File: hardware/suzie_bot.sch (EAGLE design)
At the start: 39 parts, among them IC1 LT1529CT33, IC2 L9637D, IC3 IC_TXB0108-TSSOP-20, U1 ATMEGA1284P-AU, Y1 14.7456, Y2 6.0, Y3 16.0

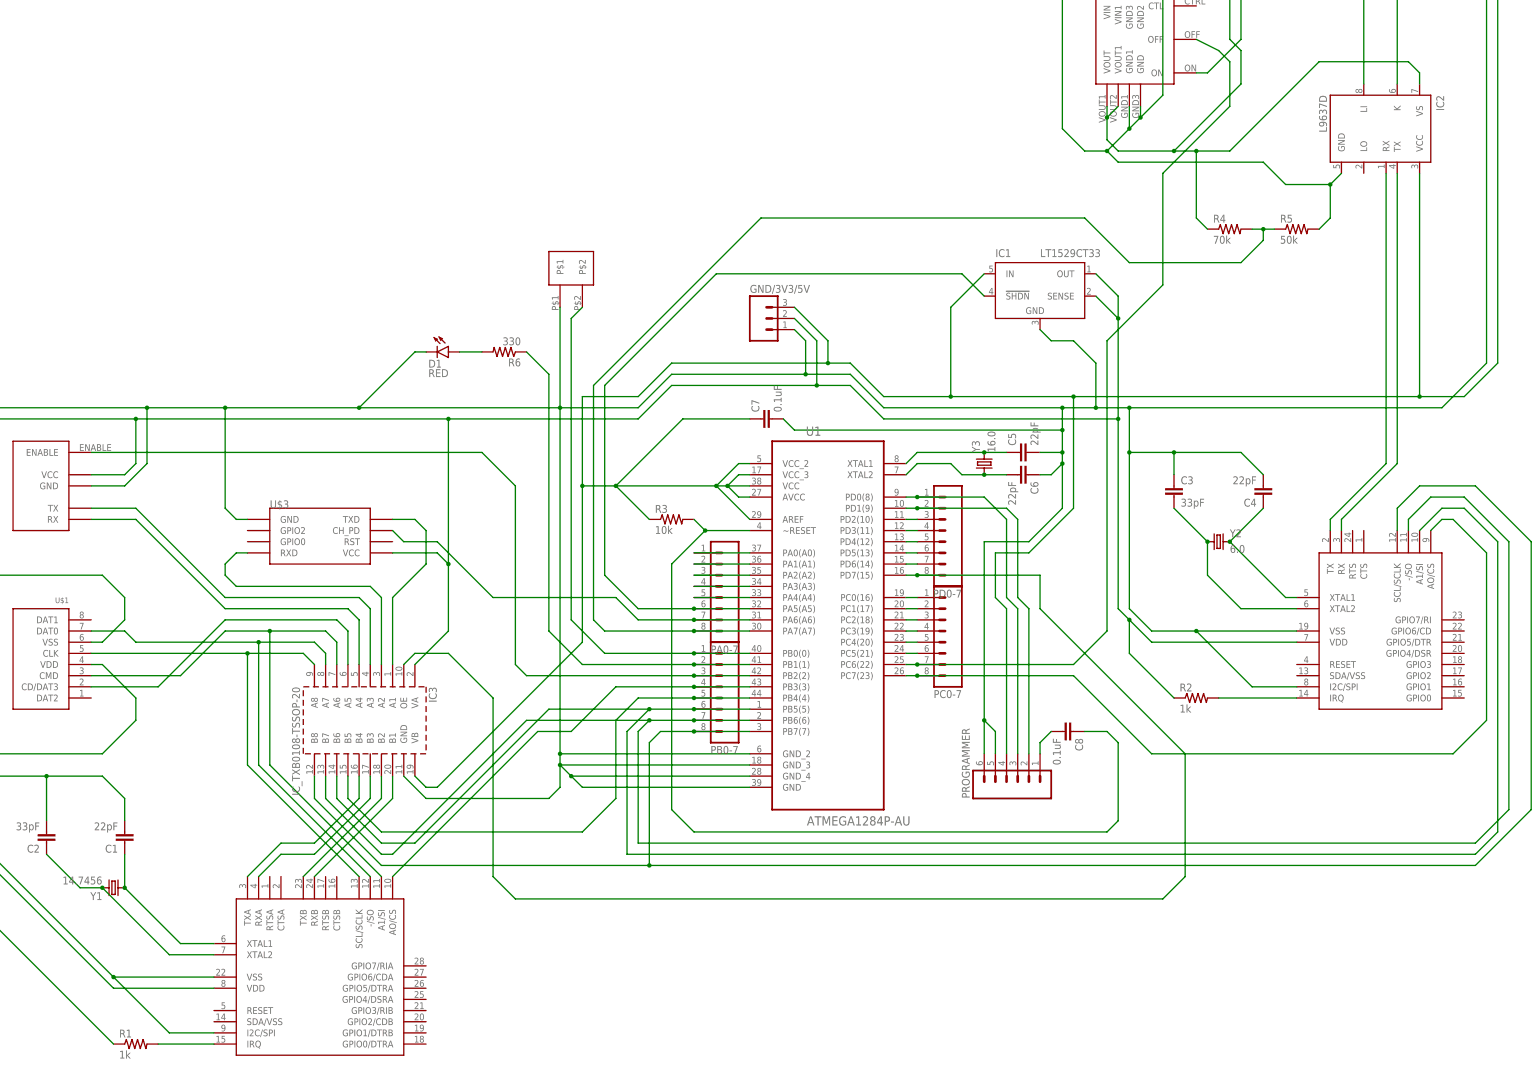
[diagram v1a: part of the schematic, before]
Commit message: Updating to v1.3 boardfile (what was once an atmega328p is now an atmega1284p)
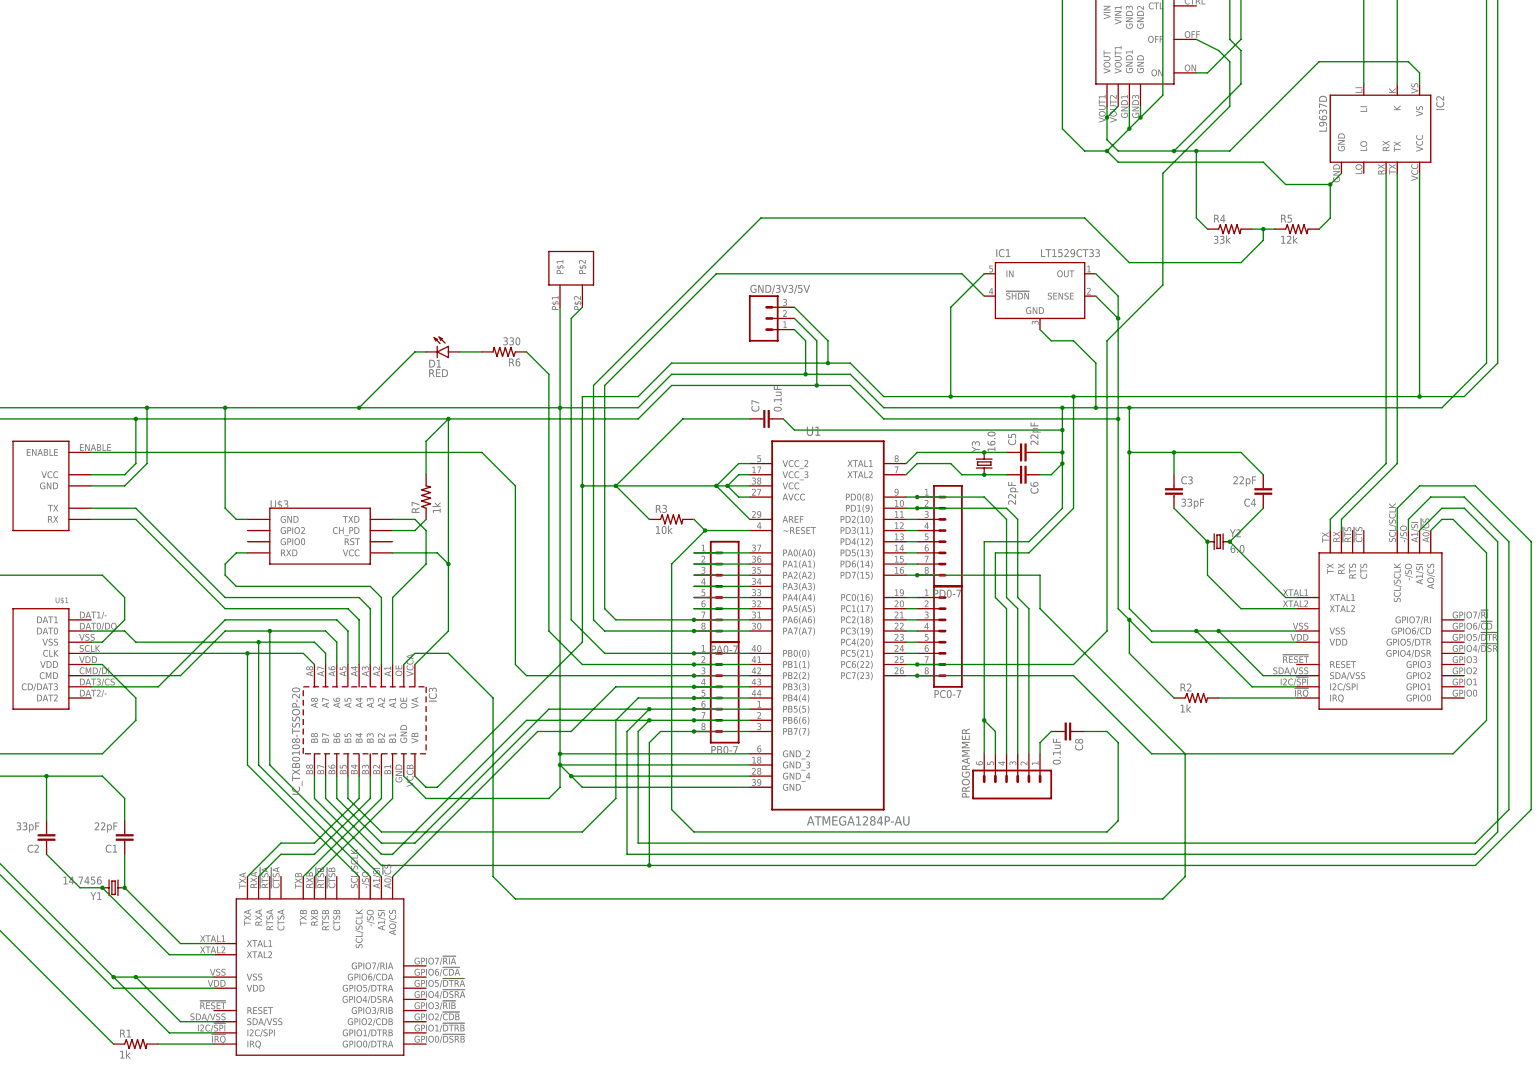
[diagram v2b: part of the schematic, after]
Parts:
- added R7: 1k, SparkFun-Passives:RESISTOR0805-RES
- R4: value 70k -> 33k
- R5: value 50k -> 12k
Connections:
- removed net PA5: IC1.!SHDN, PA0-7.6, U1.PA5(A5)
- new net N$28: PA0-7.6, U1.PA5(A5)
- new net N$4: R7.1, U$3.CH_PD
- net 3V3: now also R7.2
- net GND: now also U$2.SDA/VSS, U$7.SDA/VSS
- net PA6: now also IC1.!SHDN; no longer U$3.CH_PD
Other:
- moved on the sheet: IC2, U$1
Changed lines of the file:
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@@
 <part name="C8" library="SparkFun-Passives" deviceset="CAP" device="0805" value="0.1uF"/>
 <part name="IC3" library="dp_devices.v6" deviceset="IC_TXB0108" device="-TSSOP-20"/>
-<part name="R4" library="SparkFun-Passives" deviceset="RESISTOR" device="0805-RES" value="70k"/>
-<part name="R5" library="SparkFun-Passives" deviceset="RESISTOR" device="0805-RES" value="50k"/>
+<part name="R4" library="SparkFun-Passives" deviceset="RESISTOR" device="0805-RES" value="33k"/>
+<part name="R5" library="SparkFun-Passives" deviceset="RESISTOR" device="0805-RES" value="12k"/>
 <part name="U$1" library="dp_devices.v6" deviceset="CON_MICROSD" device="HINGED"/>
 <part name="D1" library="SparkFun-LED" deviceset="LED" device="5MM" value="RED"/>
 <part name="R6" library="SparkFun-Passives" deviceset="RESISTOR" device="0805-RES" value="330"/>
+<part name="R7" library="SparkFun-Passives" deviceset="RESISTOR" device="0805-RES" value="1k"/>
 </parts>
 <sheets>
@@
 <instance part="D1" gate="G$1" x="-76.2" y="208.28" rot="R270"/>
 <instance part="R6" gate="G$1" x="-63.5" y="208.28" rot="R180"/>
+<instance part="R7" gate="G$1" x="-81.28" y="175.26" rot="R90"/>
 </instances>
 <busses>
@@
 <wire x1="-154.94" y1="116.84" x2="-185.42" y2="116.84" width="0.1524" layer="91"/>
 <junction x="-185.42" y="116.84"/>
+<pinref part="R7" gate="G$1" pin="2"/>
+<wire x1="-81.28" y1="180.34" x2="-81.28" y2="187.96" width="0.1524" layer="91"/>
+<wire x1="-81.28" y1="187.96" x2="-76.2" y2="193.04" width="0.1524" layer="91"/>
 </segment>
 </net>
@@
 <junction x="-144.78" y="195.58"/>
 <pinref part="U$2" gate="G$1" pin="VSS"/>
-<wire x1="-129.54" y1="66.04" x2="-152.4" y2="66.04" width="0.1524" layer="91"/>
+<wire x1="-129.54" y1="66.04" x2="-147.32" y2="66.04" width="0.1524" layer="91"/>
+<wire x1="-147.32" y1="66.04" x2="-152.4" y2="66.04" width="0.1524" layer="91"/>
 <wire x1="-152.4" y1="66.04" x2="-182.88" y2="96.52" width="0.1524" layer="91"/>
 <pinref part="C1" gate="G$1" pin="2"/>
@@
 <junction x="93.98" y="144.78"/>
 <pinref part="U$7" gate="G$1" pin="VSS"/>
-<wire x1="116.84" y1="144.78" x2="93.98" y2="144.78" width="0.1524" layer="91"/>
+<wire x1="116.84" y1="144.78" x2="99.06" y2="144.78" width="0.1524" layer="91"/>
 <junction x="78.74" y="195.58"/>
+<wire x1="99.06" y1="144.78" x2="93.98" y2="144.78" width="0.1524" layer="91"/>
 <wire x1="78.74" y1="195.58" x2="71.12" y2="195.58" width="0.1524" layer="91"/>
 <wire x1="71.12" y1="195.58" x2="63.5" y2="195.58" width="0.1524" layer="91"/>
@@
 <wire x1="-83.82" y1="208.28" x2="-96.52" y2="195.58" width="0.1524" layer="91"/>
 <junction x="-96.52" y="195.58"/>
+<pinref part="U$2" gate="G$1" pin="SDA/VSS"/>
+<wire x1="-129.54" y1="55.88" x2="-137.16" y2="55.88" width="0.1524" layer="91"/>
+<wire x1="-137.16" y1="55.88" x2="-147.32" y2="66.04" width="0.1524" layer="91"/>
+<junction x="-147.32" y="66.04"/>
+<pinref part="U$7" gate="G$1" pin="SDA/VSS"/>
+<wire x1="116.84" y1="134.62" x2="109.22" y2="134.62" width="0.1524" layer="91"/>
+<wire x1="109.22" y1="134.62" x2="99.06" y2="144.78" width="0.1524" layer="91"/>
+<junction x="99.06" y="144.78"/>
 </segment>
 </net>
@@
 </segment>
 </net>
-<net name="PA5" class="0">
-<segment>
-<pinref part="U1" gate="A" pin="PA5(A5)"/>
-<pinref part="PA0-7" gate="G$1" pin="6"/>
-<wire x1="-7.62" y1="149.86" x2="-20.32" y2="149.86" width="0.1524" layer="91"/>
-<wire x1="-20.32" y1="149.86" x2="-33.02" y2="149.86" width="0.1524" layer="91"/>
-<junction x="-20.32" y="149.86"/>
-<wire x1="-33.02" y1="149.86" x2="-40.64" y2="157.48" width="0.1524" layer="91"/>
-<wire x1="-40.64" y1="157.48" x2="-40.64" y2="200.66" width="0.1524" layer="91"/>
+<net name="PA6" class="0">
+<segment>
+<pinref part="PA0-7" gate="G$1" pin="7"/>
+<pinref part="U1" gate="A" pin="PA6(A6)"/>
+<wire x1="-7.62" y1="147.32" x2="-20.32" y2="147.32" width="0.1524" layer="91"/>
+<wire x1="-20.32" y1="147.32" x2="-38.1" y2="147.32" width="0.1524" layer="91"/>
+<junction x="-20.32" y="147.32"/>
+<wire x1="-38.1" y1="147.32" x2="-40.64" y2="149.86" width="0.1524" layer="91"/>
+<wire x1="-40.64" y1="149.86" x2="-40.64" y2="200.66" width="0.1524" layer="91"/>
 <wire x1="-40.64" y1="200.66" x2="-15.24" y2="226.06" width="0.1524" layer="91"/>
 <pinref part="IC1" gate="G$1" pin="!SHDN"/>
 <wire x1="-15.24" y1="226.06" x2="40.64" y2="226.06" width="0.1524" layer="91"/>
 <wire x1="40.64" y1="226.06" x2="45.72" y2="220.98" width="0.1524" layer="91"/>
-</segment>
-</net>
-<net name="PA6" class="0">
-<segment>
-<pinref part="U$3" gate="G$1" pin="CH_PD"/>
-<wire x1="-88.9" y1="167.64" x2="-86.36" y2="165.1" width="0.1524" layer="91"/>
-<wire x1="-86.36" y1="165.1" x2="-78.74" y2="165.1" width="0.1524" layer="91"/>
-<wire x1="-78.74" y1="165.1" x2="-66.04" y2="152.4" width="0.1524" layer="91"/>
-<wire x1="-66.04" y1="152.4" x2="-38.1" y2="152.4" width="0.1524" layer="91"/>
-<pinref part="PA0-7" gate="G$1" pin="7"/>
-<pinref part="U1" gate="A" pin="PA6(A6)"/>
-<wire x1="-7.62" y1="147.32" x2="-20.32" y2="147.32" width="0.1524" layer="91"/>
-<junction x="-20.32" y="147.32"/>
-<wire x1="-20.32" y1="147.32" x2="-33.02" y2="147.32" width="0.1524" layer="91"/>
-<wire x1="-38.1" y1="152.4" x2="-33.02" y2="147.32" width="0.1524" layer="91"/>
 </segment>
 </net>
@@
 </segment>
 </net>
+<net name="N$4" class="0">
+<segment>
+<pinref part="U$3" gate="G$1" pin="CH_PD"/>
+<wire x1="-88.9" y1="167.64" x2="-83.82" y2="167.64" width="0.1524" layer="91"/>
+<wire x1="-83.82" y1="167.64" x2="-81.28" y2="170.18" width="0.1524" layer="91"/>
+<pinref part="R7" gate="G$1" pin="1"/>
+</segment>
+</net>
+<net name="N$28" class="0">
+<segment>
+<pinref part="PA0-7" gate="G$1" pin="6"/>
+<pinref part="U1" gate="A" pin="PA5(A5)"/>
+<wire x1="-7.62" y1="149.86" x2="-20.32" y2="149.86" width="0.1524" layer="91"/>
+</segment>
+</net>
 </nets>
 </sheet>
@@
 </schematic>
 </drawing>
-<compatibility>
-<note version="6.3" minversion="6.2.2" severity="warning">
-Since Version 6.2.2 text objects can contain more than one line,
-which will not be processed correctly with this version.
-</note>
-</compatibility>
 </eagle>

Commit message: Much better decoupling; adding TI TPS2113A for limiting inrush current.
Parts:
- added C10, C11, C12, C13, C14, C15, C18, C19, C20, C21, C9: 0.1uF, SparkFun-Capacitors:CAP0603-CAP
- added C16: 22uF, SparkFun-Capacitors:CAP1206
- added C17: 1000uF, rcl:CPOL-USG
- added R8: 500, SparkFun-Passives:RESISTOR0805-RES
- added U2: TPS2113APWR, Texas Instruments_By_element14_Batch_1:TPS2113APWR
- C7: device SparkFun-Passives:CAP0805 -> SparkFun-Capacitors:CAP0603-CAP
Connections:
- removed net N$2 (its old number): PB0-7.2, R6.1, U1.PB1(1)
- removed net PA6: IC1.!SHDN, PA0-7.7, U1.PA6(A6)
- new net N$25: IC3.OE, PB0-7.2, U1.PB1(1)
- new net N$27: PA0-7.7, U1.PA6(A6)
- new net N$30: C19.1, PROGRAMMER.4, U2.IN2
- new net N$31: R8.2, U2.ILIM
- new net N$32: 5V/GND.P$2, C18.2, U2.IN1
- net 12V-OUT: now also C12.2
- net 3V3: now also C10.1, C11.1, C16.1, C20.2, C21.1, C9.1
- net 5V: now also C13.1, C14.1, C15.1, C17.+, U2.OUT; no longer 5V/GND.P$1, PROGRAMMER.4
- net EXTGND: now also C12.1
- net GND: now also 5V/GND.P$1, C10.2, C11.2, C13.2, C14.2, C15.2, C16.2, C17.-, C18.1, C19.2, C20.1, C21.2, C9.2, R8.1, U2.GND, U2.VSNS, U2.~EN; no longer 5V/GND.P$2
- net PA0: now also IC1.!SHDN
- net PD7: now also R6.1; no longer IC3.OE
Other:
- moved on the sheet: C7

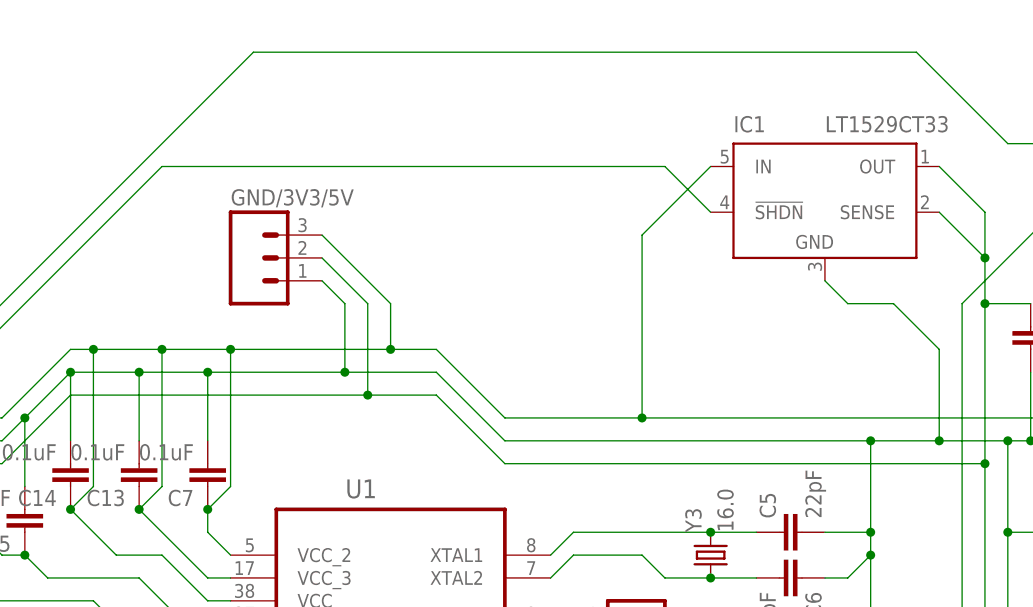
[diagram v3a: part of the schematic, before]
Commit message: Adding 1k pullup resistor for disabling 3V3 regulator until MC-enabled.
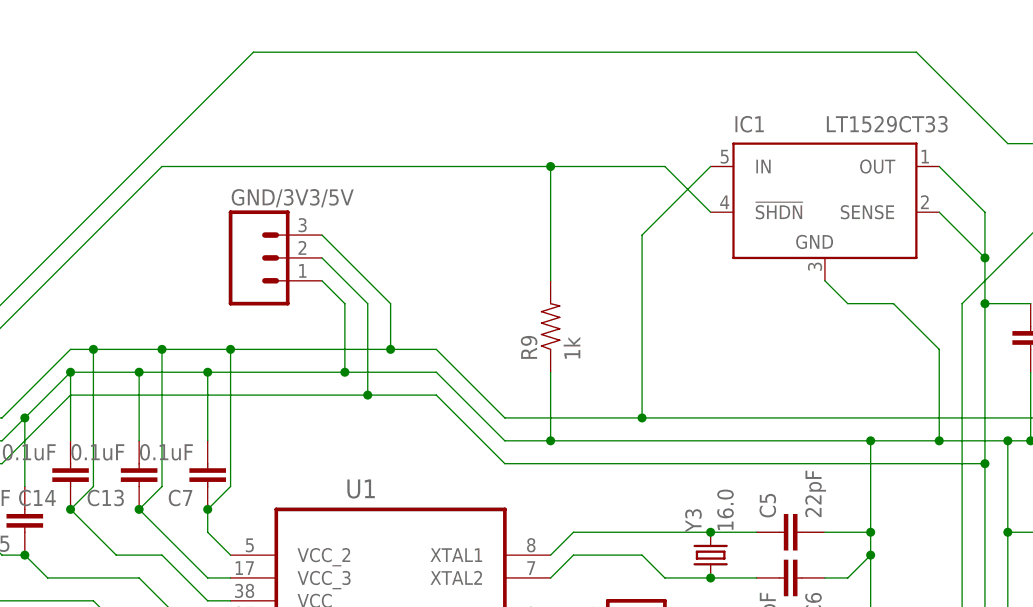
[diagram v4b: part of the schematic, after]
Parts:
- added R9: 1k, SparkFun-Passives:RESISTOR0805-RES
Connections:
- net GND: now also R9.1
- net PA0: now also R9.2
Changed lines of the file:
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@@
 <part name="C20" library="SparkFun-Capacitors" deviceset="CAP" device="0603-CAP" value="0.1uF"/>
 <part name="C21" library="SparkFun-Capacitors" deviceset="CAP" device="0603-CAP" value="0.1uF"/>
+<part name="R9" library="SparkFun-Passives" deviceset="RESISTOR" device="0805-RES" value="1k"/>
 </parts>
 <sheets>
@@
 <instance part="C20" gate="G$1" x="-147.32" y="180.34" rot="R270"/>
 <instance part="C21" gate="G$1" x="-93.98" y="180.34" rot="R270"/>
+<instance part="R9" gate="G$1" x="27.94" y="208.28" rot="R90"/>
 </instances>
 <busses>
@@
 <wire x1="71.12" y1="195.58" x2="63.5" y2="195.58" width="0.1524" layer="91"/>
 <pinref part="IC1" gate="G$1" pin="GND"/>
-<wire x1="63.5" y1="195.58" x2="22.86" y2="195.58" width="0.1524" layer="91"/>
+<wire x1="63.5" y1="195.58" x2="27.94" y2="195.58" width="0.1524" layer="91"/>
+<wire x1="27.94" y1="195.58" x2="22.86" y2="195.58" width="0.1524" layer="91"/>
 <wire x1="58.42" y1="213.36" x2="60.96" y2="210.82" width="0.1524" layer="91"/>
 <wire x1="60.96" y1="210.82" x2="66.04" y2="210.82" width="0.1524" layer="91"/>
@@
 <wire x1="-96.52" y1="180.34" x2="-96.52" y2="195.58" width="0.1524" layer="91"/>
 <junction x="-96.52" y="195.58"/>
+<pinref part="R9" gate="G$1" pin="1"/>
+<wire x1="27.94" y1="203.2" x2="27.94" y2="195.58" width="0.1524" layer="91"/>
+<junction x="27.94" y="195.58"/>
 </segment>
 </net>
@@
 <wire x1="-40.64" y1="200.66" x2="-15.24" y2="226.06" width="0.1524" layer="91"/>
 <pinref part="IC1" gate="G$1" pin="!SHDN"/>
-<wire x1="-15.24" y1="226.06" x2="40.64" y2="226.06" width="0.1524" layer="91"/>
+<wire x1="-15.24" y1="226.06" x2="27.94" y2="226.06" width="0.1524" layer="91"/>
+<wire x1="27.94" y1="226.06" x2="40.64" y2="226.06" width="0.1524" layer="91"/>
 <wire x1="40.64" y1="226.06" x2="45.72" y2="220.98" width="0.1524" layer="91"/>
 <wire x1="-40.64" y1="200.66" x2="-40.64" y2="170.18" width="0.1524" layer="91"/>
@@
 <wire x1="-33.02" y1="162.56" x2="-20.32" y2="162.56" width="0.1524" layer="91"/>
 <junction x="-20.32" y="162.56"/>
-</segment>
-</net>
+<pinref part="R9" gate="G$1" pin="2"/>
+<wire x1="27.94" y1="213.36" x2="27.94" y2="226.06" width="0.1524" layer="91"/>
+<junction x="27.94" y="226.06"/>
+</segment>
+</net>
